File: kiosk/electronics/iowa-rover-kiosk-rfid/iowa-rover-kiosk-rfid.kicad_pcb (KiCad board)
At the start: 2 copper layers, 38.7 x 47 mm, 13 parts, among them J1 Conn_01x04, J2 Conn_01x04, U1 ID12-LA, U2 ATtiny84-20P

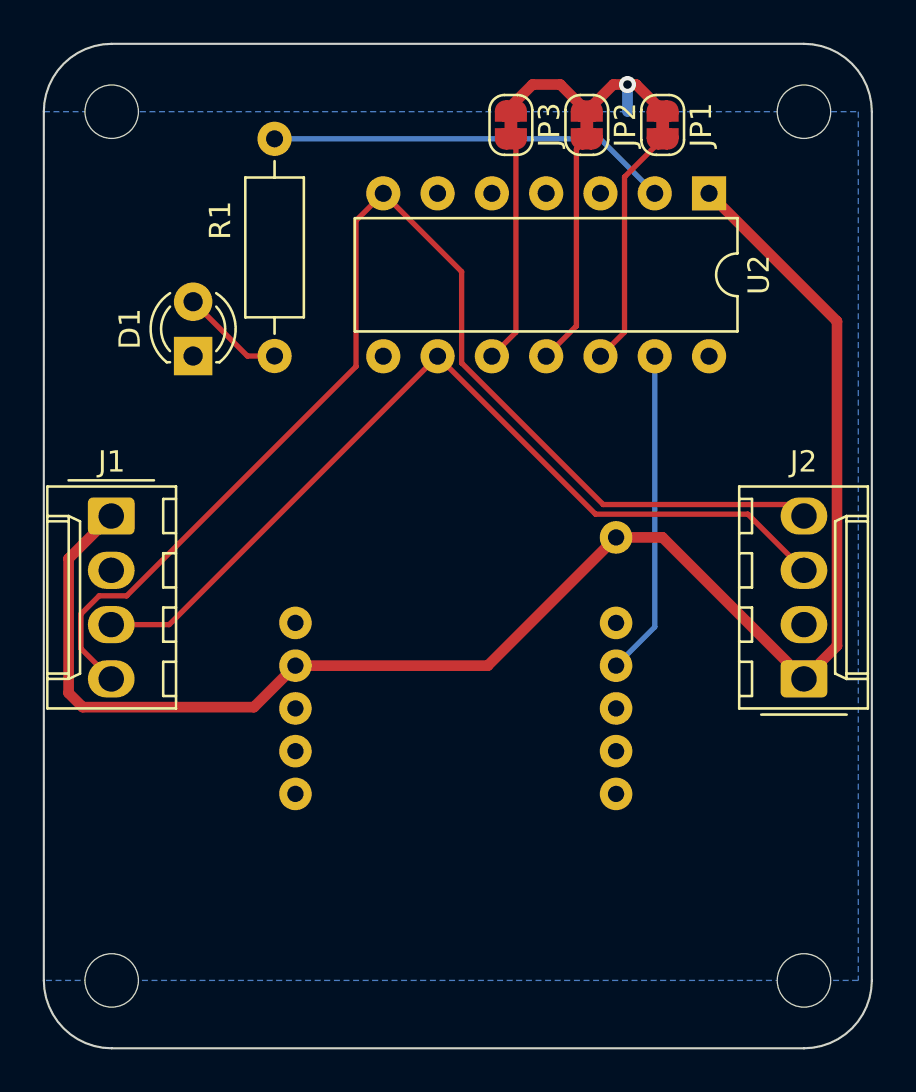
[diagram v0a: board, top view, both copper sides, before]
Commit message: fix sda/scl bus connections
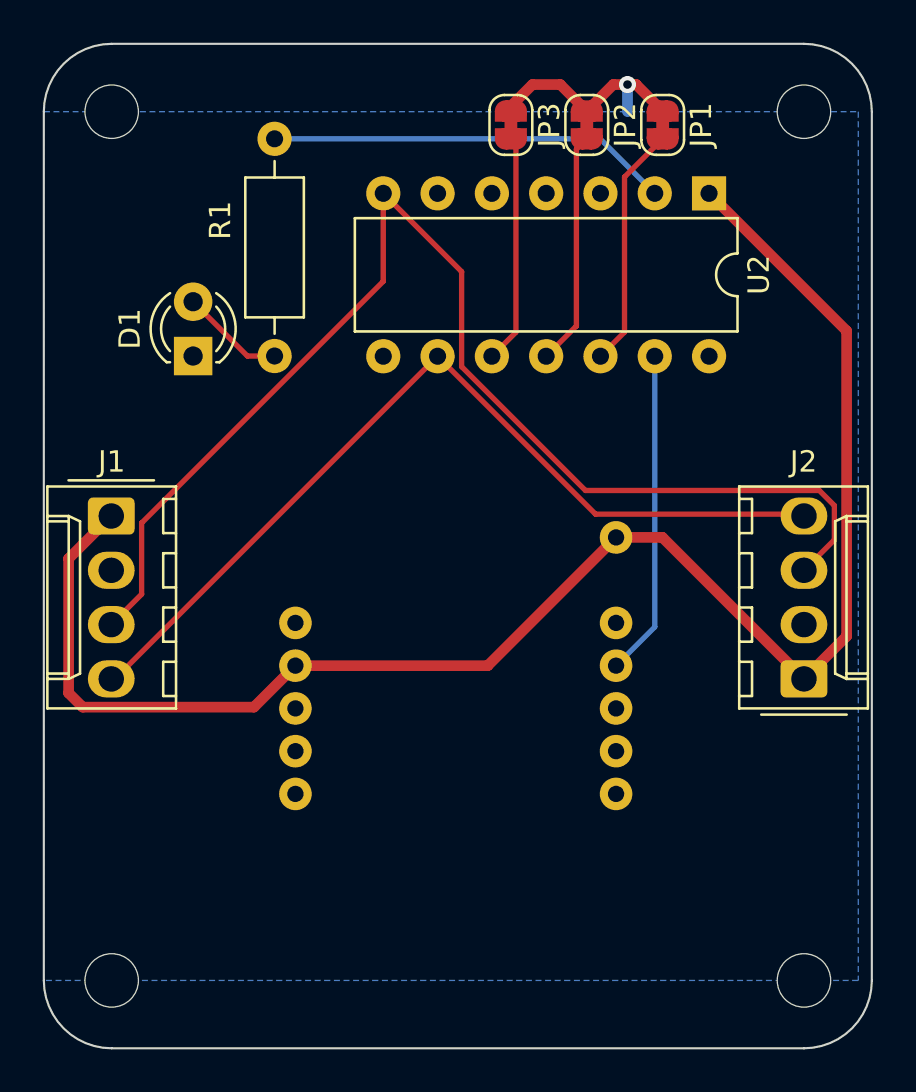
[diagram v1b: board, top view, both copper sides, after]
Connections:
- U2 pad 7: /SCL -> /SDA
- U2 pad 9: /SDA -> /SCL
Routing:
- net /SDA: track 41.8 -> 58.8 mm
- net /SCL: track 58.4 -> 41.8 mm
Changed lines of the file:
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@@
       (net 17 "unconnected-(U2-PA7-Pad6)") (pinfunction "PA7") (pintype "bidirectional+no_connect"))
     (pad "7" thru_hole oval (at 0 15.24 270) (size 1.6 1.6) (drill 0.8) (layers "*.Cu" "*.Mask")
-      (net 5 "/SCL") (pinfunction "PA6") (pintype "bidirectional"))
+      (net 4 "/SDA") (pinfunction "PA6") (pintype "bidirectional"))
     (pad "8" thru_hole oval (at 7.62 15.24 270) (size 1.6 1.6) (drill 0.8) (layers "*.Cu" "*.Mask")
       (net 18 "unconnected-(U2-PA5-Pad8)") (pinfunction "PA5") (pintype "bidirectional+no_connect"))
     (pad "9" thru_hole oval (at 7.62 12.7 270) (size 1.6 1.6) (drill 0.8) (layers "*.Cu" "*.Mask")
-      (net 4 "/SDA") (pinfunction "PA4") (pintype "bidirectional"))
+      (net 5 "/SCL") (pinfunction "PA4") (pintype "bidirectional"))
     (pad "10" thru_hole oval (at 7.62 10.16 270) (size 1.6 1.6) (drill 0.8) (layers "*.Cu" "*.Mask")
       (net 21 "Net-(JP3-B)") (pinfunction "PA3") (pintype "bidirectional"))
@@
   (segment (start 110.49 43.18) (end 109.22 43.18) (width 0.25) (layer "F.Cu") (net 2))
   (segment (start 109.22 43.18) (end 106.68 40.64) (width 0.25) (layer "F.Cu") (net 2))
-  (segment (start 135.255 58.285) (end 136.8 56.74) (width 0.5) (layer "F.Cu") (net 3))
+  (segment (start 137.25 56.29) (end 135.255 58.285) (width 0.5) (layer "F.Cu") (net 3))
   (segment (start 120.465 57.665) (end 126.465 51.665) (width 0.5) (layer "F.Cu") (net 3))
   (segment (start 100.855 58.945) (end 101.515 59.605) (width 0.5) (layer "F.Cu") (net 3))
   (segment (start 101.515 59.605) (end 109.525 59.605) (width 0.5) (layer "F.Cu") (net 3))
-  (segment (start 136.8 41.555) (end 130.815 35.57) (width 0.5) (layer "F.Cu") (net 3))
   (segment (start 128.635 51.665) (end 135.255 58.285) (width 0.5) (layer "F.Cu") (net 3))
   (segment (start 126.465 51.665) (end 128.635 51.665) (width 0.5) (layer "F.Cu") (net 3))
+  (segment (start 137.25 42.005) (end 137.25 56.29) (width 0.5) (layer "F.Cu") (net 3))
+  (segment (start 130.815 35.57) (end 137.25 42.005) (width 0.5) (layer "F.Cu") (net 3))
   (segment (start 100.855 52.66) (end 100.855 58.945) (width 0.5) (layer "F.Cu") (net 3))
   (segment (start 109.525 59.605) (end 111.465 57.665) (width 0.5) (layer "F.Cu") (net 3))
-  (segment (start 136.8 56.74) (end 136.8 41.555) (width 0.5) (layer "F.Cu") (net 3))
   (segment (start 111.465 57.665) (end 120.465 57.665) (width 0.5) (layer "F.Cu") (net 3))
   (segment (start 102.85 50.665) (end 100.855 52.66) (width 0.5) (layer "F.Cu") (net 3))
-  (segment (start 105.56 55.745) (end 118.115 43.19) (width 0.25) (layer "F.Cu") (net 4))
-  (segment (start 132.628 50.578) (end 135.255 53.205) (width 0.25) (layer "F.Cu") (net 4))
-  (segment (start 102.85 55.745) (end 105.56 55.745) (width 0.25) (layer "F.Cu") (net 4))
-  (segment (start 118.115 43.19) (end 125.503 50.578) (width 0.25) (layer "F.Cu") (net 4))
-  (segment (start 125.503 50.578) (end 132.628 50.578) (width 0.25) (layer "F.Cu") (net 4))
-  (segment (start 101.43 56.865) (end 101.43 55.250015) (width 0.25) (layer "F.Cu") (net 5))
-  (segment (start 114.3 43.669985) (end 114.3 36.845) (width 0.25) (layer "F.Cu") (net 5))
-  (segment (start 114.3 36.845) (end 115.575 35.57) (width 0.25) (layer "F.Cu") (net 5))
-  (segment (start 134.718 50.128) (end 125.862009 50.128) (width 0.25) (layer "F.Cu") (net 5))
-  (segment (start 103.569985 54.4) (end 114.3 43.669985) (width 0.25) (layer "F.Cu") (net 5))
-  (segment (start 101.43 55.250015) (end 102.280015 54.4) (width 0.25) (layer "F.Cu") (net 5))
-  (segment (start 102.85 58.285) (end 101.43 56.865) (width 0.25) (layer "F.Cu") (net 5))
-  (segment (start 125.862009 50.128) (end 119.24 43.505991) (width 0.25) (layer "F.Cu") (net 5))
-  (segment (start 102.280015 54.4) (end 103.569985 54.4) (width 0.25) (layer "F.Cu") (net 5))
-  (segment (start 119.24 43.505991) (end 119.24 39.235) (width 0.25) (layer "F.Cu") (net 5))
-  (segment (start 135.255 50.665) (end 134.718 50.128) (width 0.25) (layer "F.Cu") (net 5))
-  (segment (start 119.24 39.235) (end 115.575 35.57) (width 0.25) (layer "F.Cu") (net 5))
+  (segment (start 104.27 50.990991) (end 104.27 54.325) (width 0.25) (layer "F.Cu") (net 4))
+  (segment (start 115.575 35.57) (end 115.575 39.685991) (width 0.25) (layer "F.Cu") (net 4))
+  (segment (start 104.27 54.325) (end 102.85 55.745) (width 0.25) (layer "F.Cu") (net 4))
+  (segment (start 136.675 51.785) (end 135.255 53.205) (width 0.25) (layer "F.Cu") (net 4))
+  (segment (start 115.575 35.57) (end 119.24 39.235) (width 0.25) (layer "F.Cu") (net 4))
+  (segment (start 119.24 43.678604) (end 125.031396 49.47) (width 0.25) (layer "F.Cu") (net 4))
+  (segment (start 125.031396 49.47) (end 135.974985 49.47) (width 0.25) (layer "F.Cu") (net 4))
+  (segment (start 136.675 50.170015) (end 136.675 51.785) (width 0.25) (layer "F.Cu") (net 4))
+  (segment (start 135.974985 49.47) (end 136.675 50.170015) (width 0.25) (layer "F.Cu") (net 4))
+  (segment (start 119.24 39.235) (end 119.24 43.678604) (width 0.25) (layer "F.Cu") (net 4))
+  (segment (start 115.575 39.685991) (end 104.27 50.990991) (width 0.25) (layer "F.Cu") (net 4))
+  (segment (start 118.115 43.19) (end 103.02 58.285) (width 0.25) (layer "F.Cu") (net 5))
+  (segment (start 135.168 50.578) (end 135.255 50.665) (width 0.25) (layer "F.Cu") (net 5))
+  (segment (start 125.503 50.578) (end 135.168 50.578) (width 0.25) (layer "F.Cu") (net 5))
+  (segment (start 103.02 58.285) (end 102.85 58.285) (width 0.25) (layer "F.Cu") (net 5))
+  (segment (start 118.115 43.19) (end 125.503 50.578) (width 0.25) (layer "F.Cu") (net 5))
   (segment (start 125.725 33.02) (end 128.275 35.57) (width 0.25) (layer "B.Cu") (net 6))
   (segment (start 110.49 33.02) (end 125.725 33.02) (width 0.25) (layer "B.Cu") (net 6))

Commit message: add gerbers and initial radio code
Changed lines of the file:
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@@
       (plot_on_all_layers_selection 0x0000000_00000000)
       (disableapertmacros false)
-      (usegerberextensions false)
+      (usegerberextensions true)
       (usegerberattributes true)
       (usegerberadvancedattributes true)
@@
       (plotinvisibletext false)
       (sketchpadsonfab false)
-      (subtractmaskfromsilk false)
+      (subtractmaskfromsilk true)
       (outputformat 1)
       (mirror false)
-      (drillshape 1)
+      (drillshape 0)
       (scaleselection 1)
-      (outputdirectory "")
+      (outputdirectory "gerber/")
     )
   )
@@
       (stroke (width 0.05) (type solid)) (fill none) (layer "F.CrtYd"))
     (pad "" np_thru_hole circle (at 0 0) (size 2.5 2.5) (drill 2.5) (layers "*.Cu" "*.Mask"))
-    (pad "" np_thru_hole circle (at 0 0) (size 2.5 2.5) (drill 2.5) (layers "*.Cu" "*.Mask"))
   )
   (footprint "SMM:KK-1x04" (layer "F.Cu")
@@
     (fp_line (start 8.89 2.88) (end 8.89 -2.92)
       (stroke (width 0.1) (type solid)) (layer "F.Fab"))
-    (pad "1" thru_hole roundrect (at 0 0 270) (size 1.74 2.19) (drill 1.19) (layers "*.Cu" "*.Mask") (roundrect_rratio 0.143678)
+    (pad "1" thru_hole roundrect (at 0 0 270) (size 1.74 2.19) (drill 1.19) (layers "*.Cu" "*.Mask") (roundrect_rratio 0.1436781609)
       (net 3 "+5V") (pinfunction "Pin_1") (pintype "passive"))
     (pad "2" thru_hole oval (at 2.54 0 270) (size 1.74 2.19) (drill 1.19) (layers "*.Cu" "*.Mask")
@@
       (stroke (width 0.05) (type solid)) (fill none) (layer "F.CrtYd"))
     (pad "" np_thru_hole circle (at 0 0) (size 2.5 2.5) (drill 2.5) (layers "*.Cu" "*.Mask"))
-    (pad "" np_thru_hole circle (at 0 0) (size 2.5 2.5) (drill 2.5) (layers "*.Cu" "*.Mask"))
   )
   (footprint "SMM:Resistor_L6.3mm_D2.5mm_P10.16mm_Horizontal" (layer "F.Cu")
@@
     (fp_circle (center 0 0) (end 2.75 0)
       (stroke (width 0.05) (type solid)) (fill none) (layer "F.CrtYd"))
-    (pad "" np_thru_hole circle (at 0 0) (size 2.5 2.5) (drill 2.5) (layers "*.Cu" "*.Mask"))
     (pad "" np_thru_hole circle (at 0 0) (size 2.5 2.5) (drill 2.5) (layers "*.Cu" "*.Mask"))
   )
@@
       (stroke (width 0.05) (type solid)) (fill none) (layer "F.CrtYd"))
     (pad "" np_thru_hole circle (at 0 0) (size 2.5 2.5) (drill 2.5) (layers "*.Cu" "*.Mask"))
-    (pad "" np_thru_hole circle (at 0 0) (size 2.5 2.5) (drill 2.5) (layers "*.Cu" "*.Mask"))
   )
   (footprint "Jumper:SolderJumper-2_P1.3mm_Bridged_RoundedPad1.0x1.5mm" (layer "F.Cu")
@@
     (fp_line (start 8.89 2.88) (end 8.89 -2.92)
       (stroke (width 0.1) (type solid)) (layer "F.Fab"))
-    (pad "1" thru_hole roundrect (at 0 0 90) (size 1.74 2.19) (drill 1.19) (layers "*.Cu" "*.Mask") (roundrect_rratio 0.143678)
+    (pad "1" thru_hole roundrect (at 0 0 90) (size 1.74 2.19) (drill 1.19) (layers "*.Cu" "*.Mask") (roundrect_rratio 0.1436781609)
       (net 3 "+5V") (pinfunction "Pin_1") (pintype "passive"))
     (pad "2" thru_hole oval (at 2.54 0 90) (size 1.74 2.19) (drill 1.19) (layers "*.Cu" "*.Mask")
